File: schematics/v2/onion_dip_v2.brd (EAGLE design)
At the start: 41 x 50 mm, 38 parts, among them IC2 DS2432P

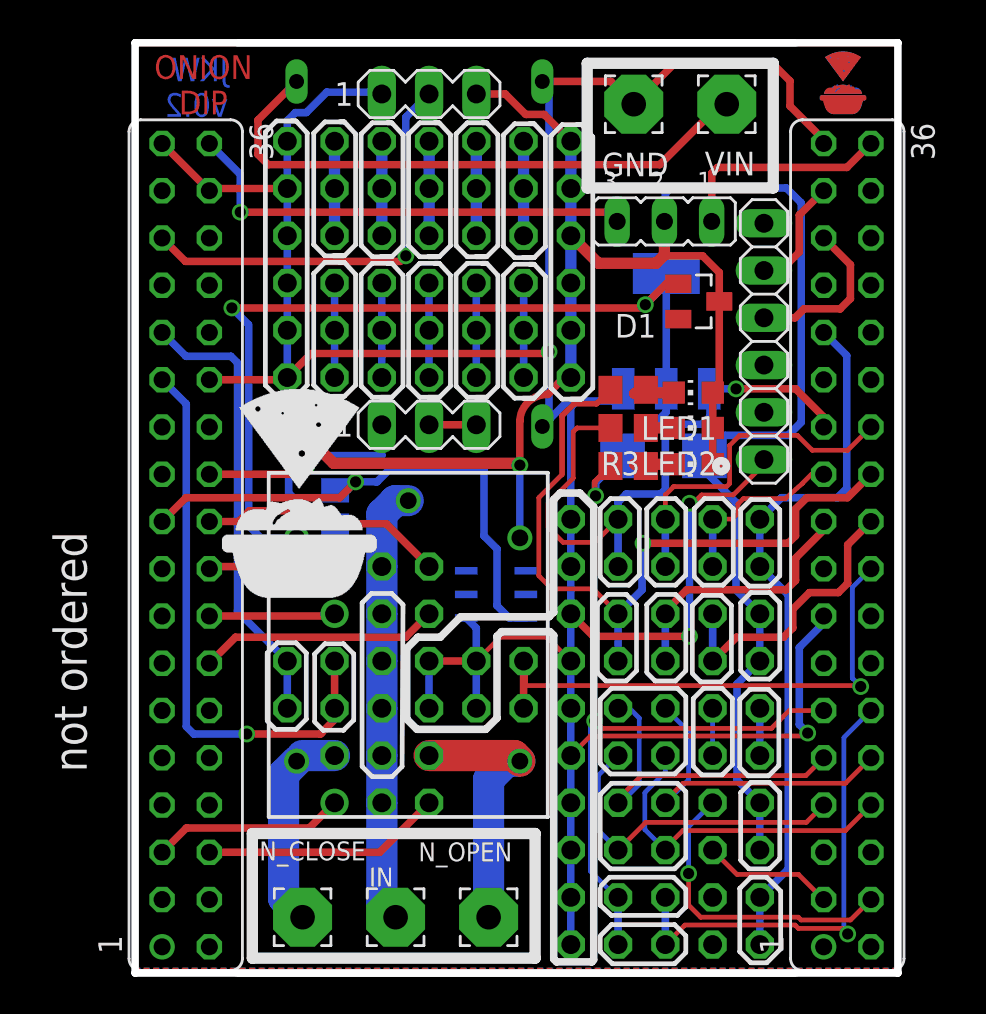
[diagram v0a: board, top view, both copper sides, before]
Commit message: increased isolation
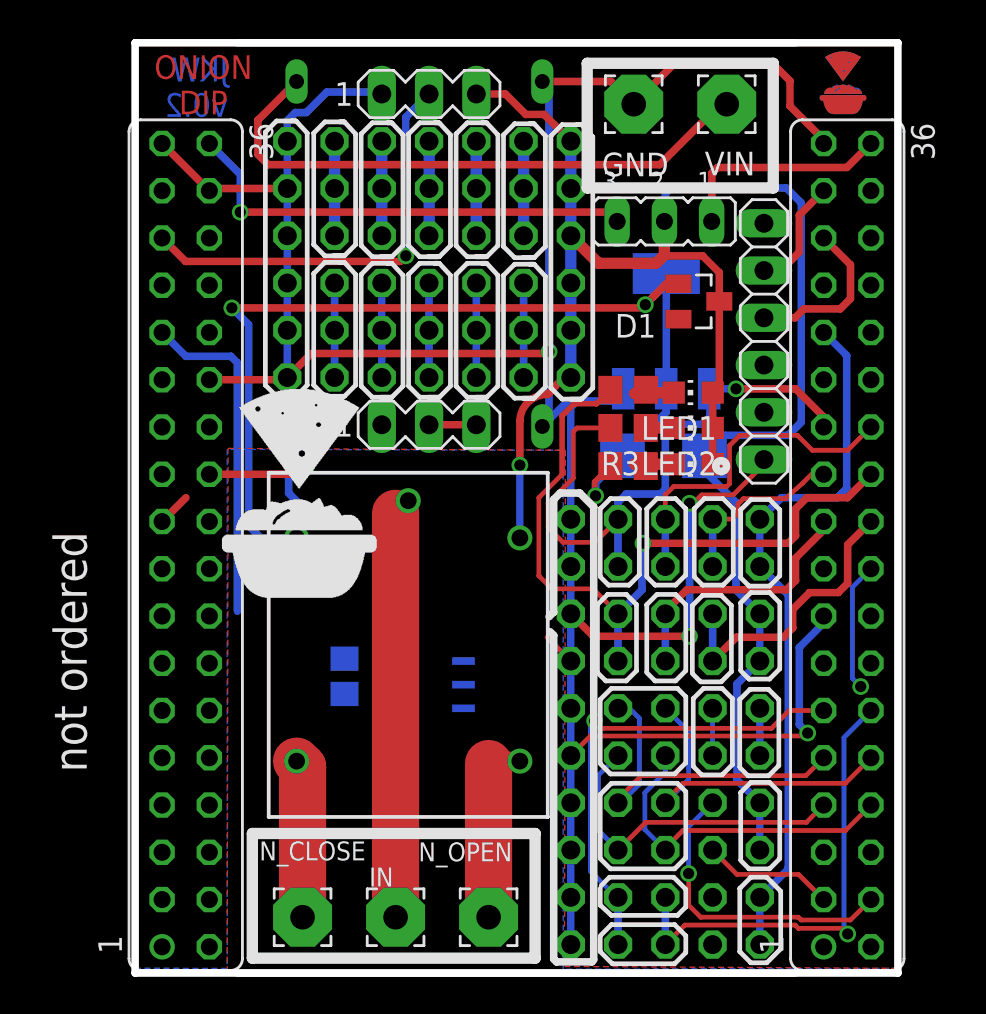
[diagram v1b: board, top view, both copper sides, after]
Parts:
- removed SV12, SV6: (no value), con-lstb_no_frame:MA03-2
- removed SV14: (no value), con-lstb_no_frame:MA06-2
- moved R1 9.06 mm to (11.2, 15.9)
- moved IC2 5.89 mm to (16.1, 15.5)
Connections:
- net GND: no longer SV14.10, SV14.7, SV14.8, SV14.9
- net LD16: no longer SV6.1
- net LD17: no longer SV6.5
- net LD3: no longer SV12.6
- net LD5: no longer SV12.2
- net LD7: no longer SV12.1
- net LD9: no longer SV12.5
- net NCL: no longer SV6.2
- net NOP: no longer SV6.6
- net P7: no longer SV14.11, SV14.12
- net RIN: no longer SV12.3, SV12.4, SV14.5, SV14.6, SV6.3, SV6.4
- net SCK: no longer SV14.3, SV14.4
- net SDA: no longer SV14.1, SV14.2
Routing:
- net SCK: track 30.8 -> 0.00 mm, vias 1 -> 0
- net LD2: track 29.2 -> 1.81 mm, vias 1 -> 0
- net P7: track 28.9 -> 7.00 mm
- net GND: track 174.6 -> 160.1 mm
- net VCC: track 122.1 -> 108.6 mm
- net LD3: track 13.3 -> 0.00 mm
- net LD17: track 12.9 -> 0.00 mm
- net LD9: track 12.9 -> 0.00 mm
- net LD16: track 10.4 -> 0.00 mm
- net LD7: track 6.78 -> 0.00 mm
- net LD5: track 6.78 -> 0.17 mm
- net SDA: track 24.4 -> 18.1 mm
- net Y2: track 11.3 -> 6.23 mm
- net NCL: track 11.3 -> 8.95 mm
- net NOP: track 14.5 -> 13.3 mm
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
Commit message: v2 routing
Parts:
- moved R1 1.19 mm to (10.2, 16.6), turned to 90 degrees
- moved IC2 0.43 mm to (16.2, 15.9), turned to 90 degrees
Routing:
- net LD2: track 1.81 -> 22.4 mm
- net VCC: track 108.6 -> 128.1 mm
- net SDA: track 18.1 -> 4.73 mm
- net Y2: track 6.23 -> 10.4 mm
- net GND: track 160.1 -> 164.1 mm
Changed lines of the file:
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@@
 <attribute name="VALUE" x="13.26" y="34.169" size="1.27" layer="27" ratio="10"/>
 </element>
-<element name="IC2" library="1wire" package="TSOC6" value="DS2432P" x="16.05" y="15.5" smashed="yes" rot="MR270">
-<attribute name="VALUE" x="19.86" y="18.04" size="1.27" layer="28" rot="MR270"/>
-</element>
-<element name="R1" library="rcl" package="R0805" value="" x="11.25" y="15.95" smashed="yes" rot="MR270">
-<attribute name="NAME" x="9.58" y="17.635" size="1.27" layer="26" rot="MR270"/>
-<attribute name="VALUE" x="13.79" y="16.585" size="1.27" layer="28" rot="MR270"/>
+<element name="IC2" library="1wire" package="TSOC6" value="DS2432P" x="16.2" y="15.9" smashed="yes" rot="MR90">
+<attribute name="VALUE" x="19.04" y="13.36" size="1.27" layer="28" rot="MR90"/>
+</element>
+<element name="R1" library="rcl" package="R0805" value="" x="10.25" y="16.6" smashed="yes" rot="MR90">
+<attribute name="NAME" x="11.92" y="14.915" size="1.27" layer="26" rot="MR90"/>
+<attribute name="VALUE" x="7.71" y="15.965" size="1.27" layer="28" rot="MR90"/>
 </element>
 <element name="D2" library="diode" package="SMB" value="" x="28.4" y="27.8" smashed="yes" rot="MR0">
@@
 <wire x1="2.73" y1="33.15" x2="5.15" y2="33.15" width="0.4064" layer="16"/>
 <wire x1="5.15" y1="33.15" x2="5.5" y2="32.8" width="0.4064" layer="16"/>
-<wire x1="5.5" y1="32.8" x2="5.5" y2="19.45" width="0.4064" layer="16"/>
 </signal>
 <signal name="SCK">
@@
 <wire x1="29.8" y1="18.1" x2="24.63" y2="18.1" width="0.4064" layer="1"/>
 <wire x1="24.63" y1="18.1" x2="23.42" y2="19.31" width="0.4064" layer="1"/>
-<wire x1="23.42" y1="16.77" x2="22.14" y2="18.05" width="0.254" layer="1"/>
 <wire x1="23.42" y1="19.31" x2="23.42" y2="16.77" width="0.4064" layer="16"/>
 <wire x1="29.8" y1="25.25" x2="30" y2="25.25" width="0.254" layer="1"/>
@@
 <wire x1="8.18" y1="34.55" x2="8.18" y2="32.01" width="0.4064" layer="16"/>
 <wire x1="23.42" y1="30.42" x2="23.75" y2="30.75" width="0.4064" layer="16"/>
-<wire x1="22.14" y1="18.05" x2="14.4498" y2="14.23" width="0" layer="19" extent="1-16"/>
+<wire x1="17.8002" y1="17.17" x2="23.02" y2="17.17" width="0.4064" layer="16"/>
+<wire x1="23.02" y1="17.17" x2="23.42" y2="16.77" width="0.4064" layer="16"/>
 </signal>
 <signal name="P5">
@@
 <contactref element="SV2" pad="19"/>
 <contactref element="IC2" pad="3"/>
-<wire x1="1.45" y1="24.27" x2="2.73" y2="25.55" width="0.4064" layer="1"/>
 <contactref element="R1" pad="1"/>
-<wire x1="11.25" y1="16.9" x2="17.6502" y2="14.23" width="0" layer="19" extent="16-16"/>
-<wire x1="2.73" y1="25.55" x2="11.25" y2="16.9" width="0" layer="19" extent="1-16"/>
+<wire x1="14.5998" y1="17.17" x2="12.72" y2="17.17" width="0.4064" layer="16"/>
+<wire x1="12.72" y1="17.17" x2="12.2" y2="16.65" width="0.4064" layer="16"/>
+<wire x1="12.2" y1="16.65" x2="12.2" y2="15.8" width="0.4064" layer="16"/>
+<wire x1="12.2" y1="15.8" x2="11.9" y2="15.5" width="0.4064" layer="16"/>
+<wire x1="11.9" y1="15.5" x2="10.4" y2="15.5" width="0.4064" layer="16"/>
+<wire x1="10.4" y1="15.5" x2="10.25" y2="15.65" width="0.4064" layer="16"/>
+<wire x1="1.45" y1="24.27" x2="1.58" y2="24.27" width="0.4064" layer="16"/>
+<wire x1="1.58" y1="24.27" x2="2.75" y2="23.1" width="0.4064" layer="16"/>
+<wire x1="2.75" y1="23.1" x2="2.75" y2="15.75" width="0.4064" layer="16"/>
+<wire x1="2.75" y1="15.75" x2="3.05" y2="15.45" width="0.4064" layer="16"/>
+<wire x1="3.05" y1="15.45" x2="10.05" y2="15.45" width="0.4064" layer="16"/>
+<wire x1="10.05" y1="15.45" x2="10.25" y2="15.65" width="0.4064" layer="16"/>
 </signal>
 <signal name="LD4">
@@
 <wire x1="3.99" y1="26.81" x2="8.81" y2="26.81" width="0.4064" layer="1"/>
 <wire x1="8.81" y1="26.81" x2="9.2" y2="27.2" width="0.4064" layer="1"/>
-<wire x1="9.81" y1="27.81" x2="9.2" y2="27.2" width="0.4064" layer="16"/>
 <contactref element="SV8" pad="1"/>
-<wire x1="9.81" y1="27.81" x2="13.26" y2="29.47" width="0" layer="19" extent="16-16"/>
+<wire x1="13.26" y1="29.47" x2="11.47" y2="29.47" width="0.4064" layer="16"/>
+<wire x1="11.47" y1="29.47" x2="9.2" y2="27.2" width="0.4064" layer="16"/>
 </signal>
 <signal name="LD3">
@@
 <wire x1="31.4" y1="36.1" x2="31.4" y2="31.55" width="0.4064" layer="1"/>
 <wire x1="31.4" y1="31.55" x2="31.05" y2="31.2" width="0.4064" layer="1"/>
-<wire x1="10" y1="24.05" x2="20.68" y2="23.39" width="0" layer="19" extent="16-16"/>
-<wire x1="11.25" y1="15" x2="10" y2="24.05" width="0" layer="19" extent="16-16"/>
+<wire x1="10" y1="24.05" x2="10" y2="17.8" width="0.4064" layer="16"/>
+<wire x1="10" y1="17.8" x2="10.25" y2="17.55" width="0.4064" layer="16"/>
+<wire x1="20.68" y1="27.3" x2="20.48" y2="27.5" width="0.4064" layer="1"/>
+<wire x1="20.48" y1="27.5" x2="10.558" y2="27.5" width="0.4064" layer="1"/>
+<wire x1="10.558" y1="27.5" x2="8.678" y2="29.38" width="0.4064" layer="1"/>
 </signal>
 <signal name="N$29">

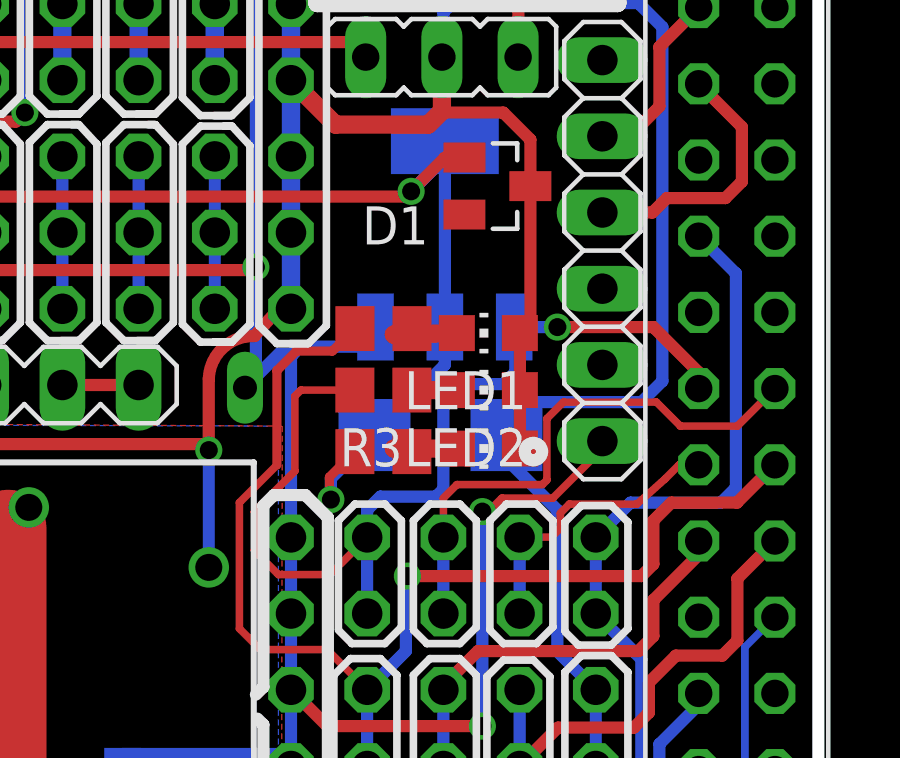
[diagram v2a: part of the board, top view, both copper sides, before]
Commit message: changed led to 3.3V and reconnected LED1 to P1 (was P0)
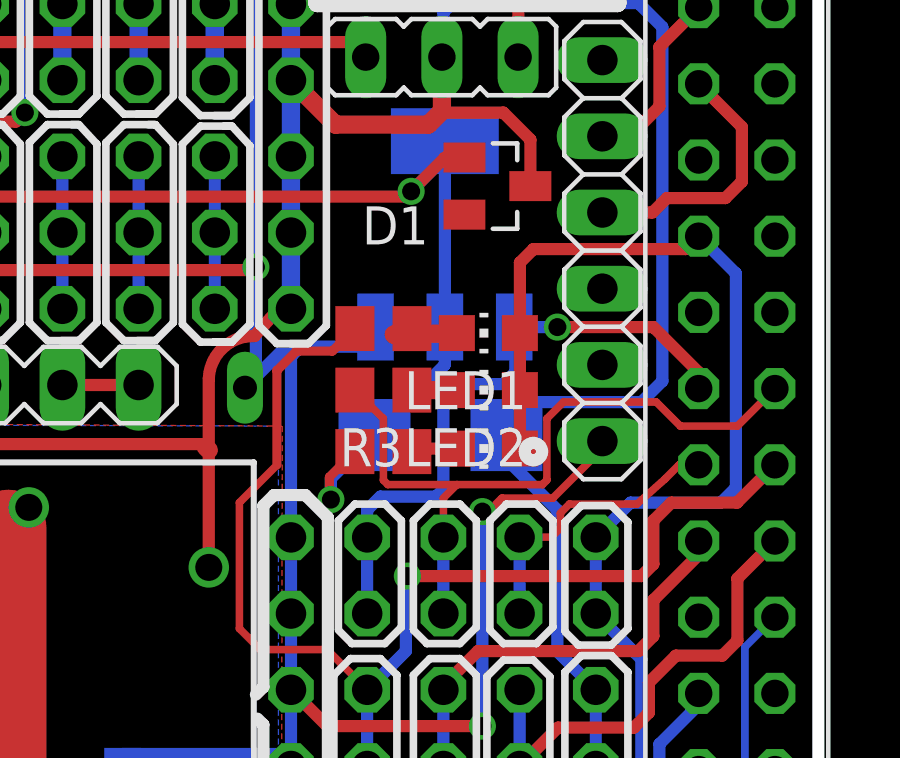
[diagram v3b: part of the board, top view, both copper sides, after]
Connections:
- net P0: no longer R3.2
- net P1: now also R3.2
- net VCC: no longer LED1.A, LED2.A, LED5.A
- net _3V3: now also LED1.A, LED2.A, LED5.A
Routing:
- net _3V3: track 38.4 -> 50.9 mm
- net P0: track 33.2 -> 20.8 mm
- net VCC: track 128.1 -> 119.2 mm, vias 1 -> 0
- net P1: track 19.3 -> 25.2 mm
- net N$29: track 2.71 -> 1.54 mm
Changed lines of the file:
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@@
 <wire x1="37.75" y1="25.55" x2="34.74" y2="25.55" width="0.4064" layer="16"/>
 <wire x1="34.74" y1="25.55" x2="33.58" y2="24.39" width="0.4064" layer="16"/>
+<contactref element="LED2" pad="A"/>
+<contactref element="LED5" pad="A"/>
+<contactref element="LED1" pad="A"/>
+<wire x1="31.05" y1="31.2" x2="31.05" y2="33.55" width="0.4064" layer="1"/>
+<wire x1="31.05" y1="33.55" x2="31.5" y2="34" width="0.4064" layer="1"/>
+<wire x1="31.5" y1="34" x2="36.58" y2="34" width="0.4064" layer="1"/>
+<wire x1="36.58" y1="34" x2="37.01" y2="34.43" width="0.4064" layer="1"/>
+<wire x1="31.05" y1="27.35" x2="31.05" y2="29.3" width="0.4064" layer="1"/>
+<wire x1="31.05" y1="29.3" x2="31.05" y2="31.2" width="0.4064" layer="1"/>
 </signal>
 <signal name="_1V8">
@@
 <wire x1="28.95" y1="26.15" x2="28.5" y2="25.7" width="0.254" layer="1"/>
 <wire x1="28.5" y1="25.7" x2="28.5" y2="23.9" width="0.254" layer="1"/>
+<contactref element="R3" pad="2"/>
+<wire x1="28.95" y1="26.15" x2="26.65" y2="26.15" width="0.254" layer="1"/>
+<wire x1="26.65" y1="26.15" x2="26.5" y2="26.3" width="0.254" layer="1"/>
+<wire x1="26.5" y1="26.3" x2="26.5" y2="28.35" width="0.254" layer="1"/>
+<wire x1="26.5" y1="28.35" x2="25.55" y2="29.3" width="0.254" layer="1"/>
 </signal>
 <signal name="AP">
@@
 <wire x1="32.3" y1="31.4" x2="30.862" y2="31.4" width="0.4064" layer="16"/>
 <wire x1="30.862" y1="31.4" x2="30.861" y2="31.401" width="0.4064" layer="16"/>
-<contactref element="R3" pad="2"/>
-<wire x1="23.55" y1="26.6" x2="22.2" y2="25.25" width="0.254" layer="1"/>
-<wire x1="22.2" y1="25.25" x2="22.2" y2="23.95" width="0.254" layer="1"/>
-<wire x1="22.2" y1="23.95" x2="23" y2="23.15" width="0.254" layer="1"/>
-<wire x1="23" y1="23.15" x2="24.72" y2="23.15" width="0.254" layer="1"/>
-<wire x1="24.72" y1="23.15" x2="25.96" y2="24.39" width="0.254" layer="1"/>
-<wire x1="23.55" y1="26.6" x2="23.55" y2="29.1" width="0.254" layer="1"/>
-<wire x1="23.55" y1="29.1" x2="23.75" y2="29.3" width="0.254" layer="1"/>
-<wire x1="23.75" y1="29.3" x2="25.55" y2="29.3" width="0.254" layer="1"/>
 </signal>
 <signal name="ADC">
@@
 <contactref element="U$1" pad="COIL1"/>
 <contactref element="D1" pad="3"/>
-<contactref element="LED5" pad="A"/>
 <contactref element="SV10" pad="10"/>
 <contactref element="SV4" pad="10"/>
@@
 <wire x1="23.42" y1="44.71" x2="23.42" y2="43.58" width="0.4064" layer="16"/>
 <wire x1="20.58" y1="27.4" x2="20.68" y2="27.3" width="0.6096" layer="1"/>
-<via x="20.68" y="27.3" extent="1-16" drill="0.6"/>
 <contactref element="R1" pad="2"/>
 <wire x1="10" y1="24.05" x2="8.25" y2="25.8" width="0.4064" layer="16"/>
@@
 <wire x1="32.35" y1="10.38" x2="32.35" y2="15.54" width="0.4064" layer="16"/>
 <wire x1="32.35" y1="15.54" x2="33.58" y2="16.77" width="0.4064" layer="16"/>
-<contactref element="LED1" pad="A"/>
-<contactref element="LED2" pad="A"/>
 <wire x1="35.1" y1="28.9" x2="35.8" y2="29.6" width="0.4064" layer="16"/>
 <wire x1="35.8" y1="29.6" x2="35.8" y2="41.4" width="0.4064" layer="16"/>
@@
 <wire x1="28.5" y1="41.9" x2="28.5" y2="40.45" width="0.4064" layer="16"/>
 <wire x1="28.5" y1="40.45" x2="28.45" y2="40.4" width="0.4064" layer="16"/>
-<wire x1="31.05" y1="29.3" x2="31.05" y2="31.2" width="0.4064" layer="1"/>
-<wire x1="31.05" y1="27.35" x2="31.05" y2="29.3" width="0.4064" layer="1"/>
 <wire x1="23.42" y1="34.17" x2="23.42" y2="34.55" width="0.6096" layer="16"/>
 <wire x1="23.42" y1="34.55" x2="23.42" y2="37.09" width="0.6096" layer="16"/>
@@
 <contactref element="SV7" pad="14"/>
 <wire x1="23.42" y1="34.55" x2="23.42" y2="32.01" width="0.6096" layer="16"/>
-<wire x1="20.68" y1="23.39" x2="20.68" y2="27.3" width="0.4064" layer="16"/>
+<wire x1="20.68" y1="23.39" x2="20.68" y2="27.3" width="0.4064" layer="1"/>
 <wire x1="18.34" y1="47.25" x2="19.9" y2="47.25" width="0.4064" layer="1"/>
 <wire x1="19.9" y1="47.25" x2="21" y2="46.15" width="0.4064" layer="1"/>
@@
 <wire x1="30.5" y1="38.55" x2="28.5" y2="38.55" width="0.4064" layer="1"/>
 <wire x1="28.5" y1="38.55" x2="28.45" y2="38.6" width="0.4064" layer="1"/>
-<wire x1="31.4" y1="36.1" x2="31.4" y2="31.55" width="0.4064" layer="1"/>
-<wire x1="31.4" y1="31.55" x2="31.05" y2="31.2" width="0.4064" layer="1"/>
 <wire x1="10" y1="24.05" x2="10" y2="17.8" width="0.4064" layer="16"/>
 <wire x1="10" y1="17.8" x2="10.25" y2="17.55" width="0.4064" layer="16"/>
@@
 <contactref element="R7" pad="1"/>
 <contactref element="LED5" pad="C"/>
-<wire x1="28.95" y1="27.35" x2="26.85" y2="27.35" width="0.6096" layer="1"/>
-<wire x1="26.85" y1="27.35" x2="27.45" y2="27.25" width="0.6096" layer="1"/>
+<wire x1="28.95" y1="27.35" x2="27.55" y2="27.35" width="0.4064" layer="1"/>
+<wire x1="27.55" y1="27.35" x2="27.45" y2="27.25" width="0.4064" layer="1"/>
 </signal>
 <signal name="CHR_IN">
